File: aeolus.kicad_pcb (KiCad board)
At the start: 4 copper layers, 120 x 25 mm, 61 parts, among them J1 Barrel_Jack_Switch, J2 Conn_01x04_Pin, J3 Conn_01x04_Pin, J4 Conn_01x04_Pin, Q1 2N3904, U1 XIAO-ESP32-C6-SMD, U2 MPM3610GQV-P, U3 LM66100DCK, U4 EMC2101-ACZL-TR, U5 INA219BIDR, U6 74LVC3G07

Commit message: feat(bom): create production files
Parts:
- removed the REF** at (198.0, 97.4)
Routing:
- net +12V: track 33.5 -> 29.9 mm, vias 4 -> 25
- net GND: track 43.7 -> 42.2 mm, vias 74 -> 73
- net /DC_IN: vias 0 -> 17
- added copper zone on B.Cu, net +12V
- added copper zone on In1.Cu, net +12V
- added copper zone on B.Cu, net /DC_IN
- added copper zone on In1.Cu, net /DC_IN
- added copper zone on In2.Cu, net /DC_IN
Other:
- board text added: "12V"
- board text added: "3V3"
- board text added: "5V"
- board text added: "A0"
- board text added: "A1"
- board text added: "Aeolus Fan Control Board"
- board text added: "REV 1.0"
- board text added: "SCL"
- board text added: "SDA"
- board text added: "TACH1"
- board text added: "TACH2"
- board text added: "TACH3"
- board text added: "VCC"

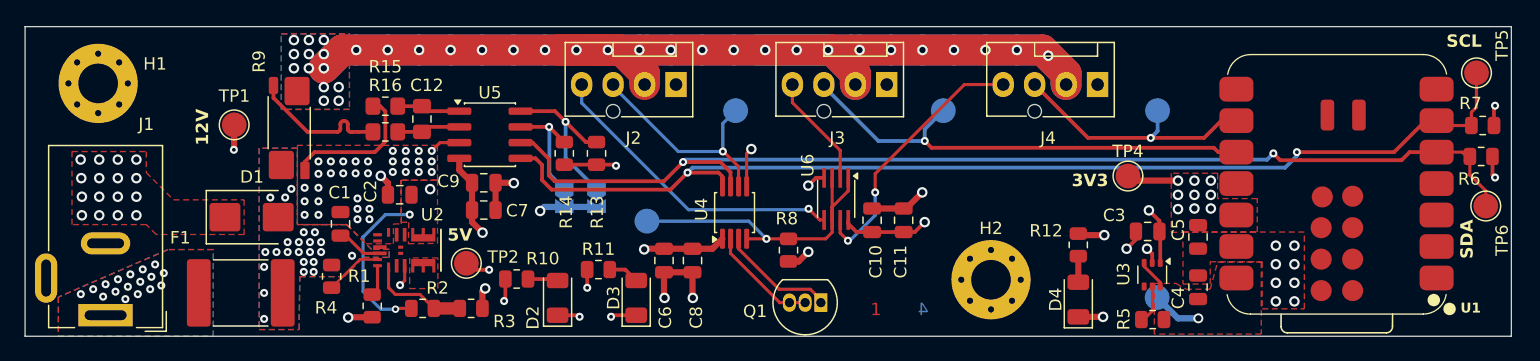
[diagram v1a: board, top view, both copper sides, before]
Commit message: fix(barrel jack): Fixed the fact that it was the wrong way around
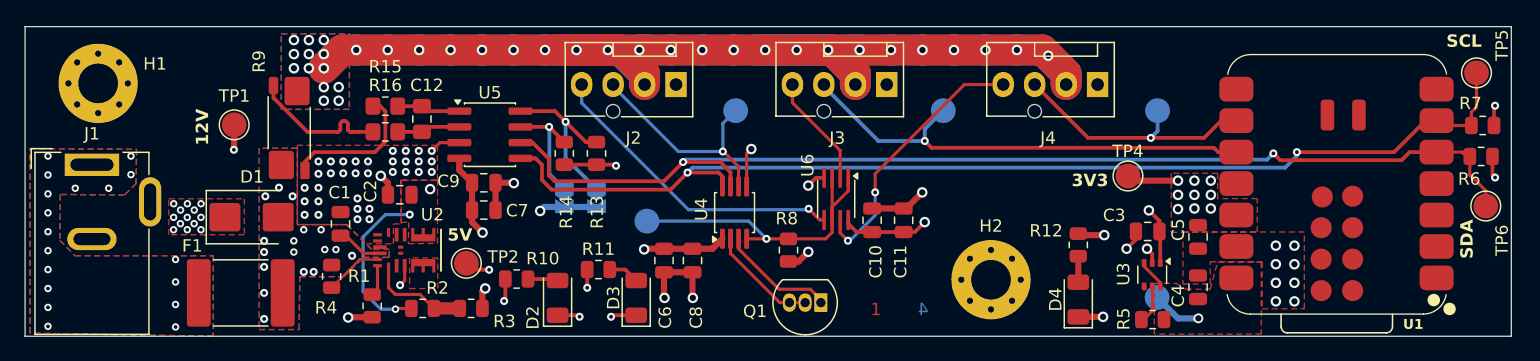
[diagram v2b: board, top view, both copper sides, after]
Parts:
- F1: value 2920L400/15MR -> 0ZCF0400FF2A; footprint Fuse:Fuse_2920_7451Metric -> Aeolus:Fuse_2920_7451Metric
- J1: footprint Connector_BarrelJack:BarrelJack_Wuerth_6941xx301002 -> Aeolus:BarrelJack_Wuerth_6941xx301002
- moved J1 12.2 mm to (124.7, 95.2), turned to 0 degrees
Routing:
- net VDC: track 218.5 -> 297.1 mm
- net +12V: track 29.9 -> 31.1 mm, vias 25 -> 19
- net GND: vias 73 -> 70
- net /DC_IN: vias 17 -> 18

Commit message: refactor: tweak design to be better for manufacturing
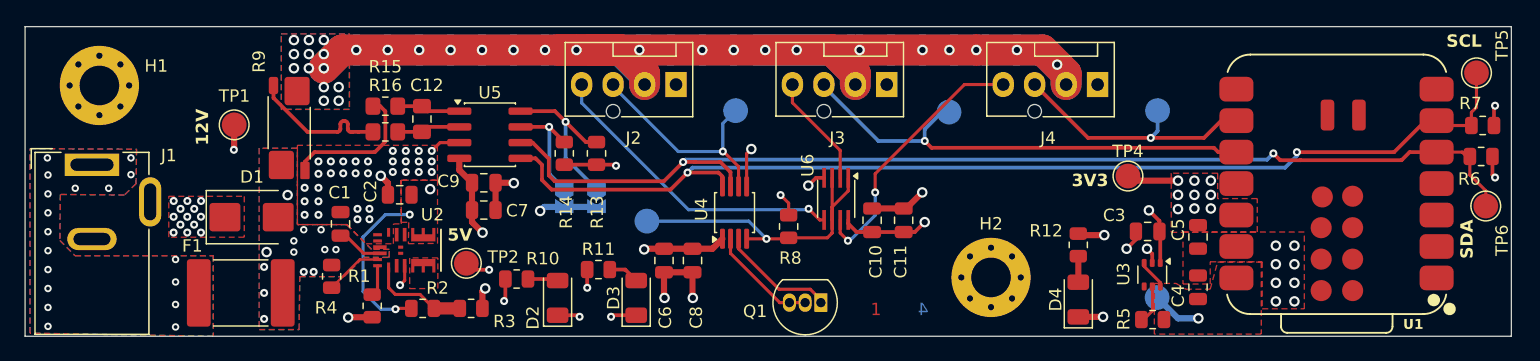
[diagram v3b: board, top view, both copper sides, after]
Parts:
- moved R8 1.91 mm to (181.0, 100.2), turned to -90 degrees
- moved TP10 0.48 mm to (193.9, 90.9)
- moved H1 0.19 mm to (125.3, 88.8)
- moved H2 0.18 mm to (197.3, 104.3)
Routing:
- net +12V: track 31.1 -> 32.7 mm, vias 19 -> 15
- net VDC: vias 36 -> 32
- net GND: vias 70 -> 69

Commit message: refactor: use ina238 rather than ina219
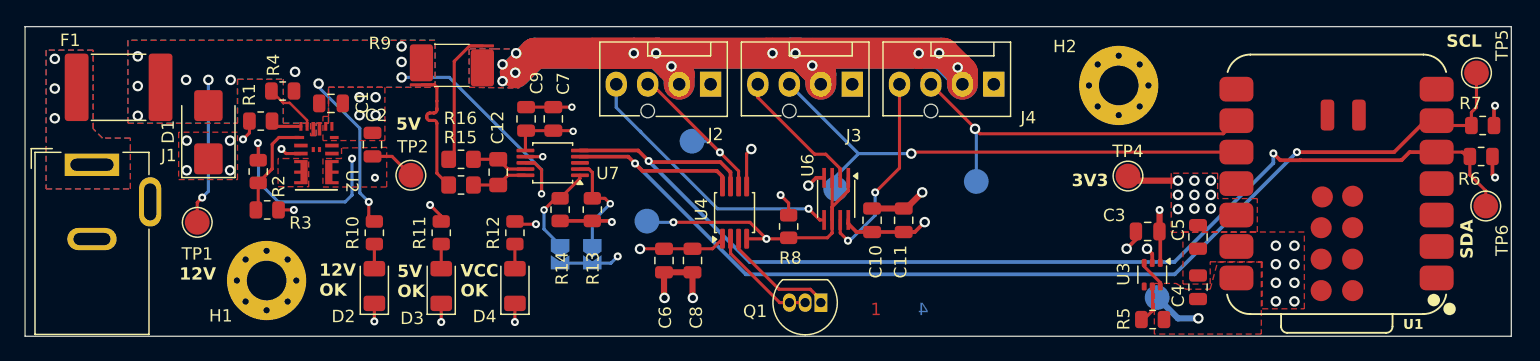
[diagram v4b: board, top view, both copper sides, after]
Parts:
- removed the REF** at (230.4, 105.1)
- removed U5: INA219BIDR, Package_SO:SOIC-8_3.9x4.9mm_P1.27mm
- added U7: INA238, Package_SO:VSSOP-10_3x3mm_P0.5mm, F.Cu at (161.9, 95.0)
- R15, R16: value 0 -> 10
- R9: value CMS-R050-1.0 -> CSNL2512FT7L00; footprint Resistor_SMD:R_Shunt_Vishay_WSK2512_6332Metric_T1.19mm -> Aeolus:Stackpole_Shunt_2512_Kelvin_7mOhm
- moved D4 45.5 mm to (158.9, 105.0)
- moved R12 45.5 mm to (158.9, 100.7)
- moved H1 20.7 mm to (138.8, 104.5)
- moved F1 19.3 mm to (126.9, 88.9)
- moved H2 18.6 mm to (207.6, 88.8)
- moved R3 18.3 mm to (138.9, 98.8)
- moved R1 17.4 mm to (138.3, 91.6), turned to 180 degrees
- moved R2 17.3 mm to (138.1, 95.7), turned to -90 degrees
- moved D3 15.8 mm to (152.9, 105.0)
- moved TP9 15.7 mm to (196.1, 96.5)
- moved R4 15.5 mm to (140.1, 89.2), turned to 180 degrees
- moved D2 14.8 mm to (147.5, 105.0)
- moved R9 14.1 mm to (153.8, 87.1), turned to 0 degrees
- moved R11 13.0 mm to (152.9, 100.7), turned to -90 degrees
- moved R10 12.1 mm to (147.5, 100.7), turned to -90 degrees
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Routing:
- net VDC: track 297.1 -> 182.3 mm, vias 32 -> 13
- net VCC: track 19.3 -> 69.3 mm
- net +12V: track 32.7 -> 44.7 mm, vias 15 -> 14
- net TACH3: track 21.1 -> 31.1 mm
- net +5V: track 86.8 -> 92.5 mm, vias 6 -> 5
- net FAN3: track 21.7 -> 16.4 mm
- net GND: track 42.2 -> 37.2 mm, vias 69 -> 32
- net Net-(JP2-A): track 13.6 -> 8.79 mm
- net SCL: track 89.3 -> 93.9 mm
- net TACH1: track 18.3 -> 14.1 mm
- net TACH2: track 39.1 -> 42.1 mm
- net SDA: track 90.1 -> 93.0 mm
- net FAN1: track 25.0 -> 22.5 mm
- net Net-(JP1-A): track 9.56 -> 7.60 mm
- net FAN2: track 9.13 -> 10.8 mm
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- added copper zone on In2.Cu, net +12V
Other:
- board text added: "12V OK"
- board text added: "5V OK"
- board text added: "VCC OK"

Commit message: refactor: more tweaking of pcb
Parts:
- removed R12: 10k, Resistor_SMD:R_0805_2012Metric
- moved TP1 1.15 mm to (133.3, 101.0)
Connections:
- D4 pad 2: Net-(D4-A) -> /VCC_OK
- R5 pad 2: Net-(U3-ST) -> /VCC_OK
- U3 pad 5: Net-(U3-ST) -> /VCC_OK
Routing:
- net VDC: track 182.3 -> 0.00 mm, vias 13 -> 17
- net VCC: track 69.3 -> 6.47 mm, vias 2 -> 1
- net /VCC_OK: track 0.00 -> 58.7 mm, vias 0 -> 2
- net +12V: track 44.7 -> 39.3 mm, vias 14 -> 20
- net Net-(U3-ST): track 3.03 -> 0.00 mm
- net +5V: track 92.5 -> 94.8 mm
- net Net-(D4-A): track 1.99 -> 0.00 mm
- net FAN: track 25.7 -> 27.4 mm, vias 2 -> 1
- net GND: track 37.2 -> 35.7 mm, vias 32 -> 30
- net TACH2: track 42.1 -> 43.1 mm
- net +3V3: track 33.9 -> 33.2 mm
- net SDA: track 93.0 -> 92.4 mm
- net /DC_IN: vias 3 -> 4

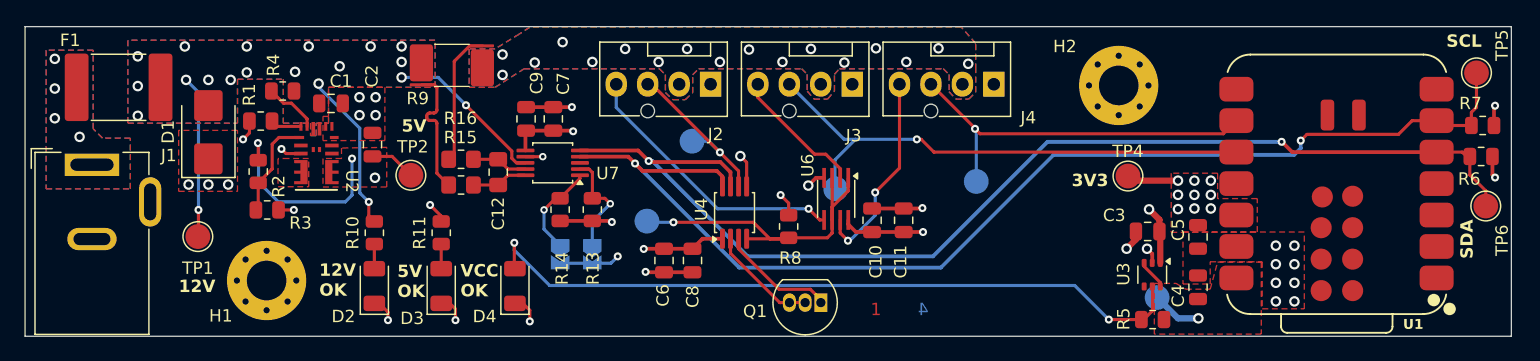
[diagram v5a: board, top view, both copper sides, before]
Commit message: feat: add qwiik connectors to board
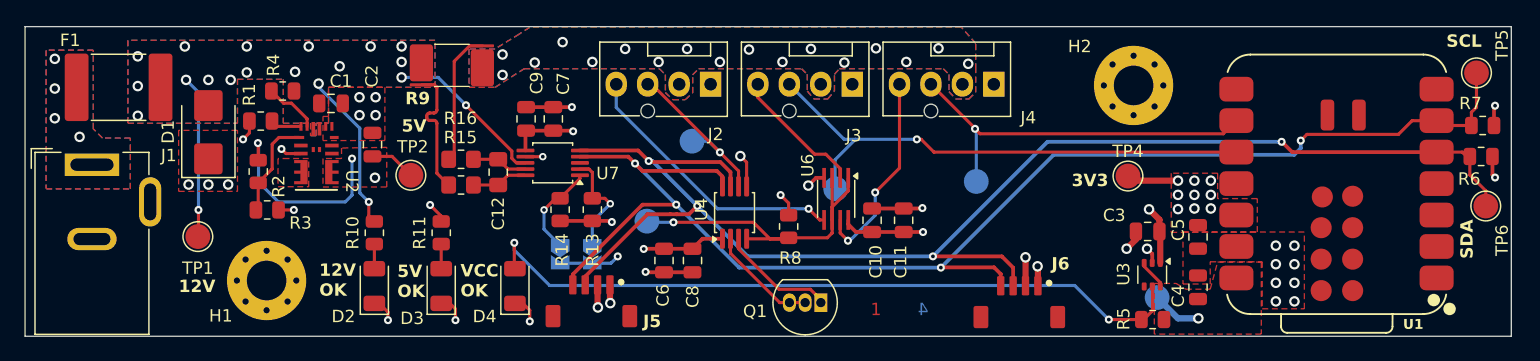
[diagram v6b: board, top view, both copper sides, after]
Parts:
- added J5: Conn_01x04_Pin, Aeolus:JST BM04B-SRSS-TB(LF)(SN)_4xP1.00mm, F.Cu at (165.0, 106.6)
- added J6: Conn_01x04_Pin, Aeolus:JST BM04B-SRSS-TB(LF)(SN)_4xP1.00mm, F.Cu at (199.6, 106.7)
- moved H2 1.20 mm to (208.8, 88.8)
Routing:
- net SDA: track 92.4 -> 112.8 mm, vias 2 -> 4
- net SCL: track 93.8 -> 111.4 mm, vias 2 -> 4
- net +3V3: track 33.2 -> 37.3 mm, vias 16 -> 18
- net GND: track 35.7 -> 38.7 mm, vias 30 -> 32

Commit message: refactor: update Qwiic connector CAD model and footprint
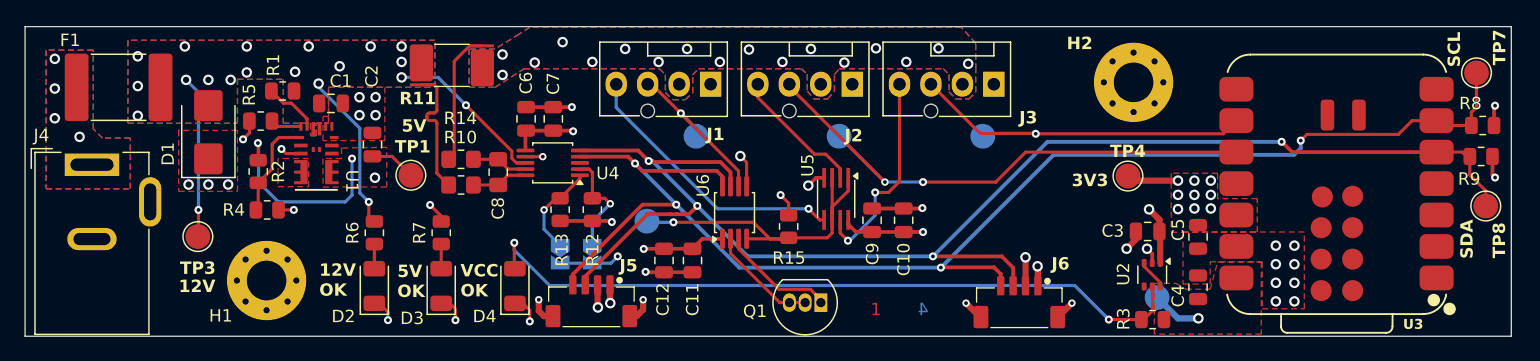
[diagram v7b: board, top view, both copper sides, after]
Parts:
- J5, J6: value Conn_01x04_Pin -> Conn_01x04_MountingPin
- moved TP5 4.26 mm to (185.0, 92.9)
- moved TP6 3.69 mm to (196.6, 92.9)
- moved TP10 0.52 mm to (173.5, 92.9)
- moved H2 0.25 mm to (208.8, 88.5)
- renumbered C11 to C10, C8 to C11, C6 to C12, C9 to C6, C12 to C8, C10 to C9, J2 to J1, J3 to J2, J4 to J3, J1 to J4, R4 to R1, R15 to R10, R9 to R11, R13 to R12, R14 to R13, R16 to R14, R8 to R15, R5 to R3, R3 to R4, R1 to R5, R10 to R6, R11 to R7, R7 to R8, R6 to R9, TP2 to TP1, TP8 to TP10, TP3 to TP2, TP1 to TP3, TP10 to TP5, TP9 to TP6, TP5 to TP7, TP6 to TP8, TP7 to TP9, U2 to U1, U3 to U2, U1 to U3, U7 to U4, U6 to U5, U4 to U6
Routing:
- net GND: track 38.7 -> 46.3 mm, vias 32 -> 36
- net TACH2: track 43.1 -> 45.7 mm, vias 1 -> 2
- net FAN3: track 16.4 -> 17.0 mm
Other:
- board text added: "FAN"
- board text added: "INA238 Addr. Select"

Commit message: style: added OSHW and Qwiic Logos to PCB and Schematic
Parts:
- added #SYM1: OSHW-Symbol_6.7x6mm_SilkScreen, Symbol:OSHW-Symbol_6.7x6mm_SilkScreen, B.Cu at (232.4, 102.8)
- added G1: LOGO, Qwiic_Logo:qwiic_5.5mm, F.Cu at (196.4, 102.5)
- added G2: LOGO, Qwiic_Logo:qwiic_5.5mm, F.Cu at (163.4, 102.5)
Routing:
- net +12V: track 39.3 -> 40.3 mm
